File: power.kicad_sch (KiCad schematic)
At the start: 28 parts, among them Q1 CSD16340Q3, Q2 CSD17311Q5, U10 INA260, U11 DS4432U+, U12 TPS40305

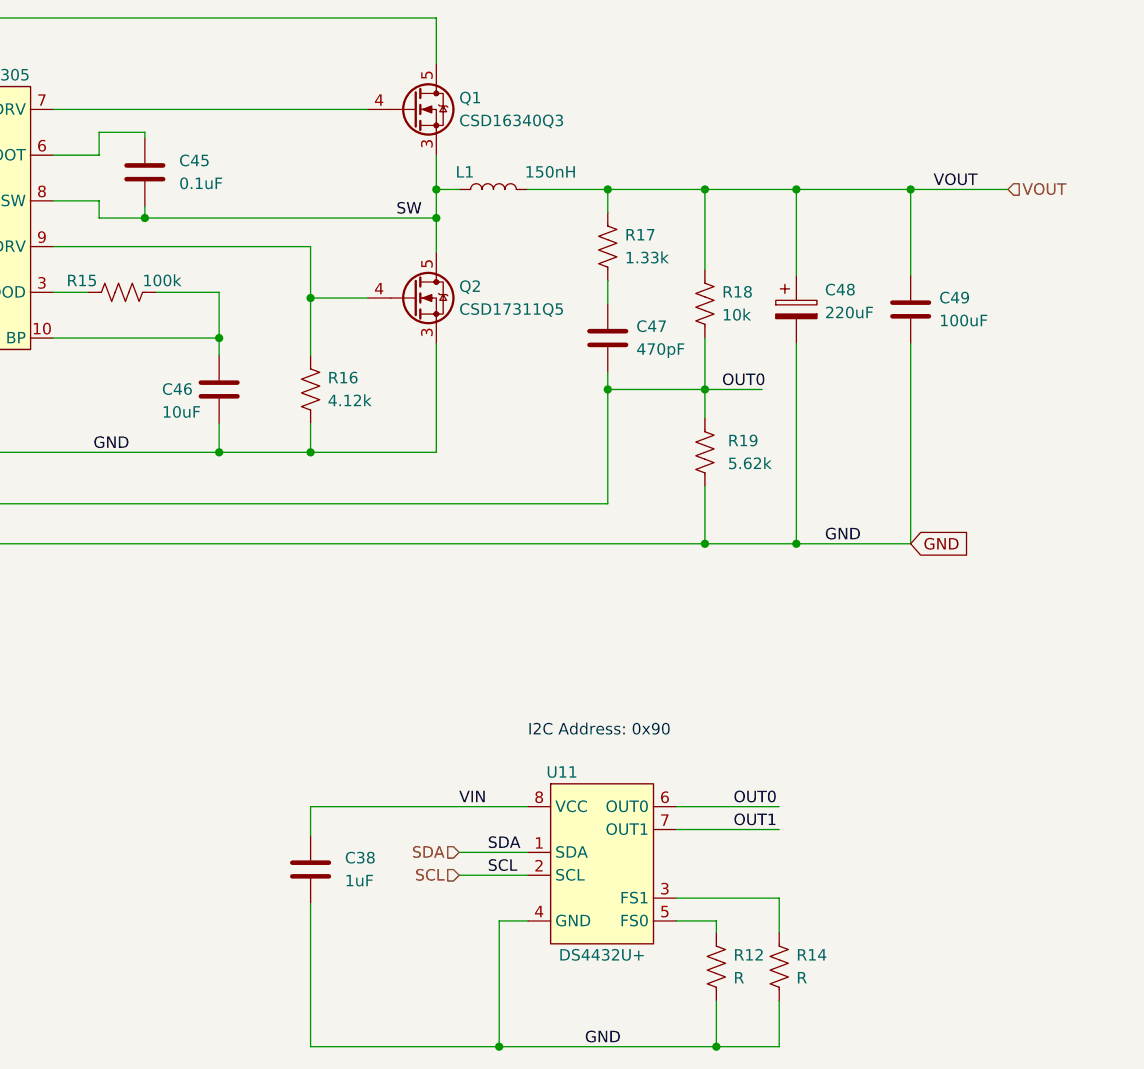
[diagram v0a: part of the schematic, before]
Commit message: switched over to the ESP32-S3 module. added a bunch of TODO notes
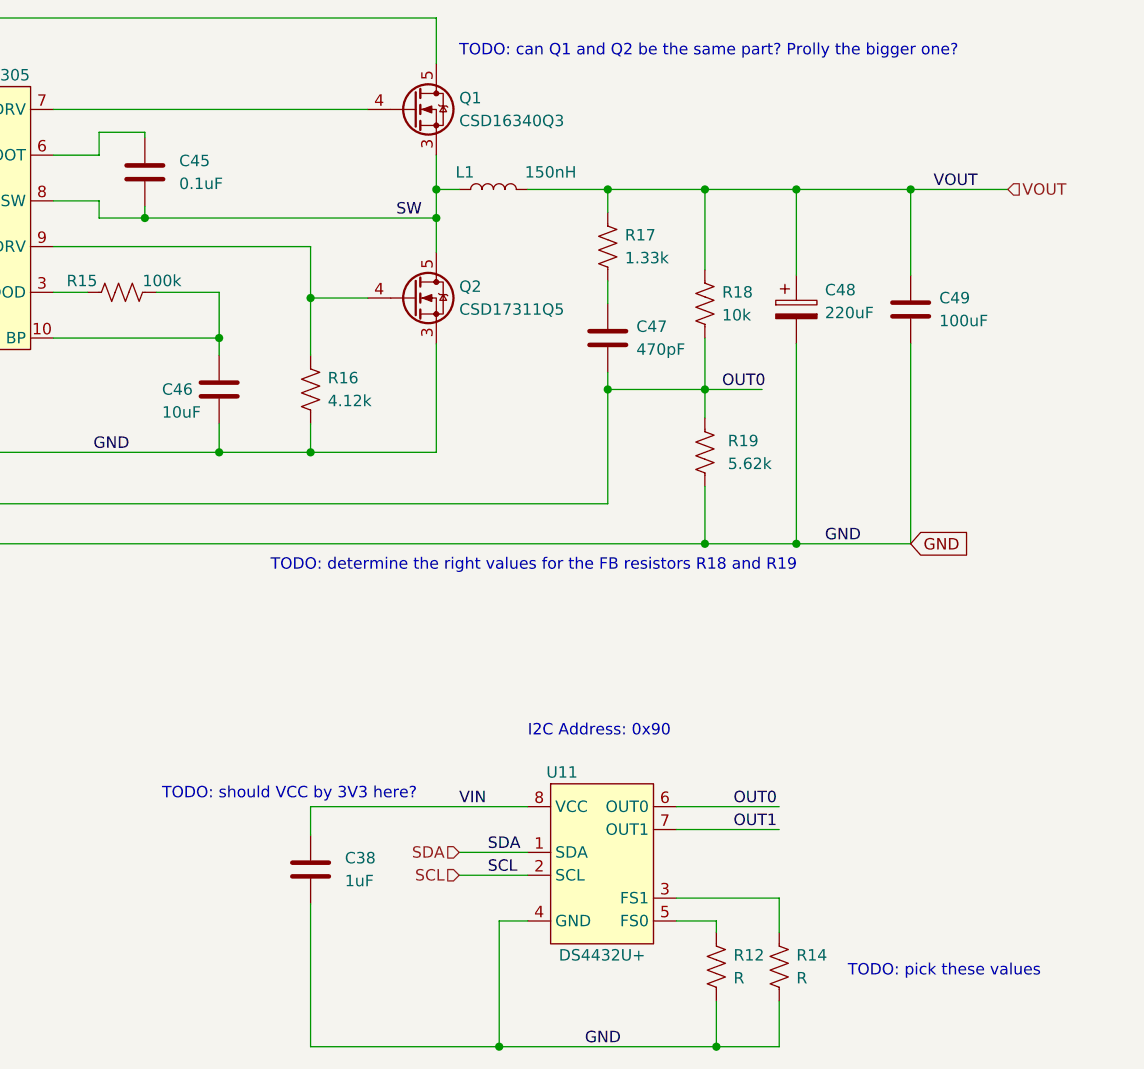
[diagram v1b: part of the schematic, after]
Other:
- note added: "TODO: can Q1 and Q2 be the same part? Prolly the bigger one?"
- note added: "TODO: determine the right values for the FB resistors R18 and R19"
- note added: "TODO: pick these values"
- note added: "TODO: should VCC by 3V3 here?"
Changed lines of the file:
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@@
+    (effects (font (size 1.27 1.27)) (justify left bottom))
+  )
+  (text "TODO: pick these values" (at 252.73 130.175 0)
+    (effects (font (size 1.27 1.27)) (justify left bottom))
+  )
+  (text "TODO: should VCC by 3V3 here?" (at 176.53 110.49 0)
     (effects (font (size 1.27 1.27)) (justify left bottom))
   )
@@
     (effects (font (size 1.27 1.27)) (justify left bottom))
   )
+  (text "TODO: determine the right values for the FB resistors R18 and R19"
+    (at 188.595 85.09 0)
+    (effects (font (size 1.27 1.27)) (justify left bottom))
+  )
+  (text "TODO: can Q1 and Q2 be the same part? Prolly the bigger one?"
+    (at 209.55 27.94 0)
+    (effects (font (size 1.27 1.27)) (justify left bottom))
+  )

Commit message: mostly done
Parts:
- removed C37, C39, C40: 47uF, Capacitor_SMD:C_1210_3225Metric, symbol Device:C
- removed C41: 1uF, Capacitor_SMD:C_0805_2012Metric, symbol Device:C
- removed C42: 3.3nF, Capacitor_SMD:C_0402_1005Metric, symbol Device:C
- removed C43: 180pF, Capacitor_SMD:C_0805_2012Metric, symbol Device:C
- removed C44: 1.5nF, Capacitor_SMD:C_0805_2012Metric, symbol Device:C
- removed C45: 0.1uF, Capacitor_SMD:C_0402_1005Metric, symbol Device:C
- removed C46: 10uF, Capacitor_SMD:C_0805_2012Metric, symbol Device:C
- removed C47: 470pF, Capacitor_SMD:C_0805_2012Metric, symbol Device:C
- removed C48: 220uF, TPS40305_supply:CAP_2R5TPE220MAFB, symbol Device:C_Polarized
- removed C49: 100uF, Capacitor_SMD:C_1206_3216Metric, symbol Device:C
- removed R13: 3.83k, Resistor_SMD:R_0402_1005Metric, symbol Device:R_US
- removed R15: 100k, Resistor_SMD:R_0402_1005Metric, symbol Device:R_US
- removed R16: 4.12k, Resistor_SMD:R_0402_1005Metric, symbol Device:R_US
- removed R17: 1.33k, Resistor_SMD:R_0402_1005Metric, symbol Device:R_US
- removed R18: 10k, Resistor_SMD:R_0402_1005Metric, symbol Device:R_US
- removed R19: 5.62k, Resistor_SMD:R_0402_1005Metric, symbol Device:R_US
- removed U12: TPS40305, symbol TPS40305:TPS40305
- added C1, C2, C3: 47uF, Capacitor_SMD:C_1210_3225Metric, symbol Device:C
- added C10: 470pF, Capacitor_SMD:C_0805_2012Metric, symbol Device:C
- added C11: 220uF, TPS40305_supply:CAP_2R5TPE220MAFB, symbol Device:C_Polarized
- added C12: 100uF, Capacitor_SMD:C_1206_3216Metric, symbol Device:C
- added C4: 1uF, Capacitor_SMD:C_0805_2012Metric, symbol Device:C
- added C5: 3.3nF, Capacitor_SMD:C_0402_1005Metric, symbol Device:C
- added C6: 180pF, Capacitor_SMD:C_0805_2012Metric, symbol Device:C
- added C7: 1.5nF, Capacitor_SMD:C_0805_2012Metric, symbol Device:C
- added C8: 0.1uF, Capacitor_SMD:C_0402_1005Metric, symbol Device:C
- added C9: 10uF, Capacitor_SMD:C_0805_2012Metric, symbol Device:C
- added R1: 3.83k, Resistor_SMD:R_0402_1005Metric, symbol Device:R_US
- added R2: 100k, Resistor_SMD:R_0402_1005Metric, symbol Device:R_US
- added R3: 4.12k, Resistor_SMD:R_0402_1005Metric, symbol Device:R_US
- added R4: 1.33k, Resistor_SMD:R_0402_1005Metric, symbol Device:R_US
- added R5: 10k, Resistor_SMD:R_0402_1005Metric, symbol Device:R_US
- added R6: 5.62k, Resistor_SMD:R_0402_1005Metric, symbol Device:R_US
- added U1: TPS40305, TPS40305_supply:TPS40305, symbol TPS40305:TPS40305
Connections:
- net 5V: now also C1.1, C2.1, C3.1, C4.1, U1.1 (VDD)
- net GND: now also C1.2, C11.2, C12.2, C2.2, C3.2, C4.2, C5.2, C9.2, R3.2, R6.2, U1.11 (GND)
- net OUT0: now also C10.2, C6.2, R1.2, R5.2, R6.1, U1.5 (FB)
- net SW: now also C8.2, U1.8 (SW)
- net VOUT: now also C11.1, C12.1, R4.1, R5.1
- net at Q1.4 (G): now also U1.7 (HDRV)
- net at Q2.4 (G): now also R3.1, U1.9 (LDRV)
- new net: C9.1, R2.2, U1.10 (BP)
- new net: C5.1, U1.2 (SS)
- new net: R2.1, U1.3 (PGOOD)
- new net: C6.1, C7.1, U1.4 (COMP)
- new net: C8.1, U1.6 (BOOT)
- new net: C7.2, R1.1
- new net: C10.1, R4.2

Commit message: reset reference designators
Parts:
- renumbered C1 to C34, C36 to C35, C2 to C36, C3 to C37, C4 to C38, C5 to C39, C6 to C40, C7 to C41, C8 to C42, C9 to C43, C38 to C44, C10 to C45, C11 to C46, C12 to C47, R1 to R10, R2 to R11, R3 to R12, R4 to R13, R5 to R14, R6 to R15, R12 to R16, R14 to R17, U11 to U10, U10 to U8, U1 to U9
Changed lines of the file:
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@@
   (symbol (lib_id "Device:C") (at 157.48 59.69 0) (unit 1)
     (in_bom yes) (on_board yes) (fields_autoplaced)
-    (property "Reference" "C9" (id 0) (at 160.655 58.4199 0)
+    (property "Reference" "C43" (id 0) (at 160.655 58.4199 0)
       (effects (font (size 1.27 1.27)) (justify left))
     )
@@
   (symbol (lib_id "Device:R_US") (at 212.725 52.07 0) (unit 1)
     (in_bom yes) (on_board yes) (fields_autoplaced)
-    (property "Reference" "R5" (id 0) (at 214.63 50.7999 0)
+    (property "Reference" "R14" (id 0) (at 214.63 50.7999 0)
       (effects (font (size 1.27 1.27)) (justify left))
     )
@@
   (symbol (lib_id "Device:C") (at 62.865 40.64 0) (unit 1)
     (in_bom yes) (on_board yes) (fields_autoplaced)
-    (property "Reference" "C3" (id 0) (at 66.04 39.3699 0)
+    (property "Reference" "C37" (id 0) (at 66.04 39.3699 0)
       (effects (font (size 1.27 1.27)) (justify left))
     )
@@
   (symbol (lib_id "Device:C_Polarized") (at 222.885 52.705 0) (unit 1)
     (in_bom yes) (on_board yes) (fields_autoplaced)
-    (property "Reference" "C11" (id 0) (at 226.06 50.5459 0)
+    (property "Reference" "C46" (id 0) (at 226.06 50.5459 0)
       (effects (font (size 1.27 1.27)) (justify left))
     )
@@
   (symbol (lib_id "TPS40305:TPS40305") (at 122.555 43.18 0) (unit 1)
     (in_bom yes) (on_board yes)
-    (property "Reference" "U1" (id 0) (at 112.395 26.67 0))
+    (property "Reference" "U9" (id 0) (at 112.395 26.67 0))
     (property "Value" "TPS40305" (id 1) (at 128.27 26.67 0))
     (property "Footprint" "TPS40305_supply:TPS40305" (id 2) (at 108.585 54.61 0)
@@
   (symbol (lib_id "Sensor:INA260") (at 65.405 109.855 0) (unit 1)
     (in_bom yes) (on_board yes)
-    (property "Reference" "U10" (id 0) (at 69.85 100.965 0)
+    (property "Reference" "U8" (id 0) (at 69.85 100.965 0)
       (effects (font (size 1.27 1.27)) (justify left))
     )
@@
   (symbol (lib_id "Device:C") (at 41.275 40.64 0) (unit 1)
     (in_bom yes) (on_board yes) (fields_autoplaced)
-    (property "Reference" "C1" (id 0) (at 44.45 39.3699 0)
+    (property "Reference" "C34" (id 0) (at 44.45 39.3699 0)
       (effects (font (size 1.27 1.27)) (justify left))
     )
@@
   (symbol (lib_id "Device:C") (at 85.09 40.64 0) (unit 1)
     (in_bom yes) (on_board yes) (fields_autoplaced)
-    (property "Reference" "C5" (id 0) (at 88.265 39.3699 0)
+    (property "Reference" "C39" (id 0) (at 88.265 39.3699 0)
       (effects (font (size 1.27 1.27)) (justify left))
     )
@@
   (symbol (lib_id "Device:C") (at 52.07 40.64 0) (unit 1)
     (in_bom yes) (on_board yes) (fields_autoplaced)
-    (property "Reference" "C2" (id 0) (at 55.245 39.3699 0)
+    (property "Reference" "C36" (id 0) (at 55.245 39.3699 0)
       (effects (font (size 1.27 1.27)) (justify left))
     )
@@
   (symbol (lib_id "Device:C") (at 74.295 40.64 0) (unit 1)
     (in_bom yes) (on_board yes)
-    (property "Reference" "C4" (id 0) (at 78.105 39.3699 0)
+    (property "Reference" "C38" (id 0) (at 78.105 39.3699 0)
       (effects (font (size 1.27 1.27)) (justify left))
     )
@@
   (symbol (lib_id "TPS40305:DS4432U+") (at 226.06 117.475 0) (unit 1)
     (in_bom yes) (on_board yes)
-    (property "Reference" "U11" (id 0) (at 220.98 107.315 0))
+    (property "Reference" "U10" (id 0) (at 220.98 107.315 0))
     (property "Value" "DS4432U+" (id 1) (at 225.425 127.635 0))
     (property "Footprint" "" (id 2) (at 226.06 117.475 0)
@@
   (symbol (lib_id "Device:C") (at 235.585 52.705 0) (unit 1)
     (in_bom yes) (on_board yes) (fields_autoplaced)
-    (property "Reference" "C12" (id 0) (at 238.76 51.4349 0)
+    (property "Reference" "C47" (id 0) (at 238.76 51.4349 0)
       (effects (font (size 1.27 1.27)) (justify left))
     )
@@
   (symbol (lib_id "Device:C") (at 95.25 56.515 0) (unit 1)
     (in_bom yes) (on_board yes) (fields_autoplaced)
-    (property "Reference" "C7" (id 0) (at 98.425 55.2449 0)
+    (property "Reference" "C41" (id 0) (at 98.425 55.2449 0)
       (effects (font (size 1.27 1.27)) (justify left))
     )
@@
   (symbol (lib_id "Device:R_US") (at 212.725 68.58 0) (unit 1)
     (in_bom yes) (on_board yes) (fields_autoplaced)
-    (property "Reference" "R6" (id 0) (at 215.265 67.3099 0)
+    (property "Reference" "R15" (id 0) (at 215.265 67.3099 0)
       (effects (font (size 1.27 1.27)) (justify left))
     )
@@
   (symbol (lib_id "Device:R_US") (at 142.875 50.8 90) (unit 1)
     (in_bom yes) (on_board yes)
-    (property "Reference" "R2" (id 0) (at 138.43 49.53 90))
+    (property "Reference" "R11" (id 0) (at 138.43 49.53 90))
     (property "Value" "100k" (id 1) (at 147.32 49.53 90))
     (property "Footprint" "Resistor_SMD:R_0402_1005Metric" (id 2) (at 143.129 49.784 90)
@@
   (symbol (lib_id "Device:C") (at 145.415 37.465 0) (unit 1)
     (in_bom yes) (on_board yes) (fields_autoplaced)
-    (property "Reference" "C8" (id 0) (at 149.225 36.1949 0)
+    (property "Reference" "C42" (id 0) (at 149.225 36.1949 0)
       (effects (font (size 1.27 1.27)) (justify left))
     )
@@
   (symbol (lib_id "Device:R_US") (at 238.125 128.905 0) (unit 1)
     (in_bom yes) (on_board yes) (fields_autoplaced)
-    (property "Reference" "R12" (id 0) (at 240.03 127.6349 0)
+    (property "Reference" "R16" (id 0) (at 240.03 127.6349 0)
       (effects (font (size 1.27 1.27)) (justify left))
     )
@@
   (symbol (lib_id "Device:C") (at 193.04 118.11 0) (unit 1)
     (in_bom yes) (on_board yes)
-    (property "Reference" "C38" (id 0) (at 196.85 116.8399 0)
+    (property "Reference" "C44" (id 0) (at 196.85 116.8399 0)
       (effects (font (size 1.27 1.27)) (justify left))
     )
@@
   (symbol (lib_id "Device:R_US") (at 201.93 45.72 0) (unit 1)
     (in_bom yes) (on_board yes) (fields_autoplaced)
-    (property "Reference" "R4" (id 0) (at 203.835 44.4499 0)
+    (property "Reference" "R13" (id 0) (at 203.835 44.4499 0)
       (effects (font (size 1.27 1.27)) (justify left))
     )
@@
   (symbol (lib_id "Device:R_US") (at 95.25 65.405 0) (unit 1)
     (in_bom yes) (on_board yes) (fields_autoplaced)
-    (property "Reference" "R1" (id 0) (at 97.155 64.1349 0)
+    (property "Reference" "R10" (id 0) (at 97.155 64.1349 0)
       (effects (font (size 1.27 1.27)) (justify left))
     )
@@
   (symbol (lib_id "Device:C") (at 201.93 55.88 0) (unit 1)
     (in_bom yes) (on_board yes) (fields_autoplaced)
-    (property "Reference" "C10" (id 0) (at 205.105 54.6099 0)
+    (property "Reference" "C45" (id 0) (at 205.105 54.6099 0)
       (effects (font (size 1.27 1.27)) (justify left))
     )
@@
   (symbol (lib_id "Device:R_US") (at 245.11 128.905 0) (unit 1)
     (in_bom yes) (on_board yes) (fields_autoplaced)
-    (property "Reference" "R14" (id 0) (at 247.015 127.6349 0)
+    (property "Reference" "R17" (id 0) (at 247.015 127.6349 0)
       (effects (font (size 1.27 1.27)) (justify left))
     )
@@
   (symbol (lib_id "Device:R_US") (at 170.18 61.595 0) (unit 1)
     (in_bom yes) (on_board yes) (fields_autoplaced)
-    (property "Reference" "R3" (id 0) (at 172.085 60.3249 0)
+    (property "Reference" "R12" (id 0) (at 172.085 60.3249 0)
       (effects (font (size 1.27 1.27)) (justify left))
     )
@@
   (symbol (lib_id "Device:C") (at 42.545 110.49 0) (unit 1)
     (in_bom yes) (on_board yes)
-    (property "Reference" "C36" (id 0) (at 46.355 109.2199 0)
+    (property "Reference" "C35" (id 0) (at 46.355 109.2199 0)
       (effects (font (size 1.27 1.27)) (justify left))
     )
@@
   (symbol (lib_id "Device:C") (at 87.63 60.96 0) (unit 1)
     (in_bom yes) (on_board yes)
-    (property "Reference" "C6" (id 0) (at 81.915 60.325 0)
-      (effects (font (size 1.27 1.27)) (justify left))
-    )
+    (property "Reference" "C40" (id 0) (at 81.915 60.325 0)
+      (effects (font (size 1.27 1.27)) (justify left))
+    )

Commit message: all footprints should be added now
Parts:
- U10: footprint (none) -> Package_SO:TSSOP-8_3x3mm_P0.65mm; DK (none) -> DS4432U+-ND; PARTNO (none) -> DS4432U+
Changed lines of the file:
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@@
     (property "Reference" "U10" (id 0) (at 220.98 107.315 0))
     (property "Value" "DS4432U+" (id 1) (at 225.425 127.635 0))
-    (property "Footprint" "" (id 2) (at 226.06 117.475 0)
+    (property "Footprint" "Package_SO:TSSOP-8_3x3mm_P0.65mm" (id 2) (at 226.06 117.475 0)
       (effects (font (size 1.27 1.27)) hide)
     )
-    (property "Datasheet" "" (id 3) (at 226.06 117.475 0)
+    (property "Datasheet" "https://datasheets.maximintegrated.com/en/ds/DS4432.pdf" (id 3) (at 226.06 117.475 0)
       (effects (font (size 1.27 1.27)) hide)
     )
+    (property "DK" "DS4432U+-ND" (id 4) (at 226.06 117.475 0)
+      (effects (font (size 1.27 1.27)) hide)
+    )
+    (property "PARTNO" "DS4432U+" (id 5) (at 226.06 117.475 0)
+      (effects (font (size 1.27 1.27)) hide)
+    )

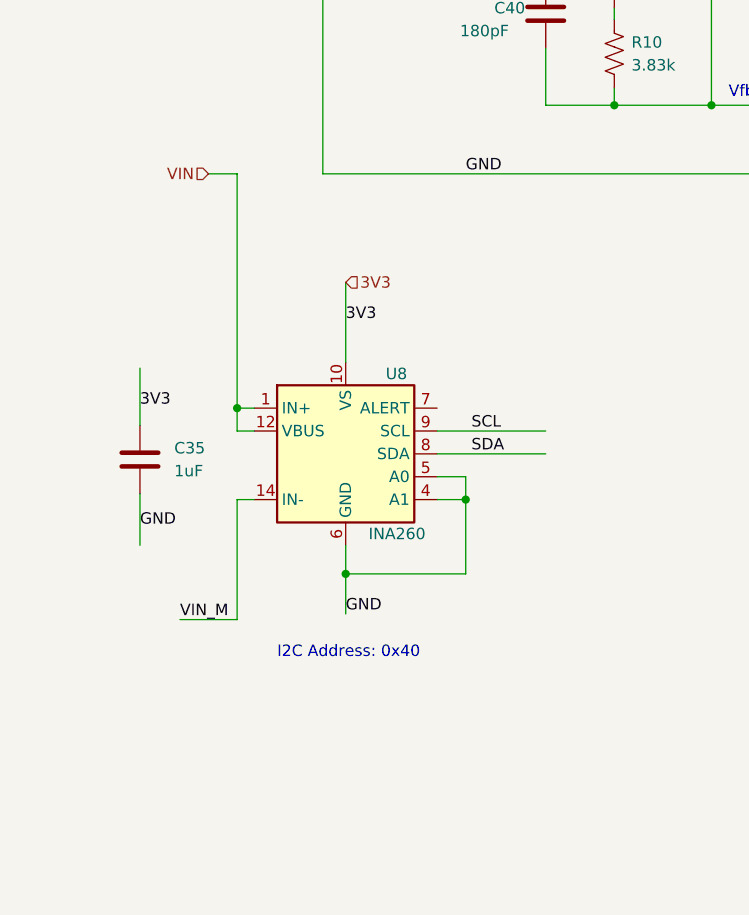
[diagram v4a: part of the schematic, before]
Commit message: library and schematic cleanup
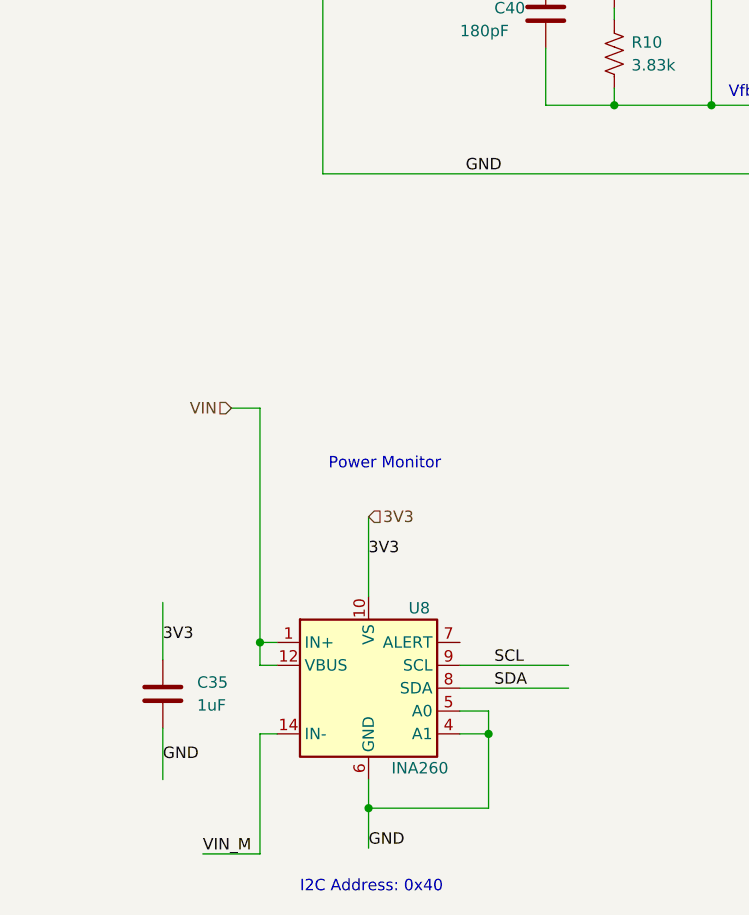
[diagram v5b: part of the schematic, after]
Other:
- note added: "Power Monitor"
- moved on the sheet: C35, U8
